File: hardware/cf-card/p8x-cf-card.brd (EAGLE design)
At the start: 160 x 100 mm, 27 parts, among them J1 DIN41612-96M, J2 CF/IDE 40P, U1 DATA BUF, U2 IO PAGE, U3 DOE DEC, U4 DLD DEC, U5 74HCT14, U6 74HCT10, U7 74HCT10, U8 74HCT08, U9 CF HI-BYTE DNP

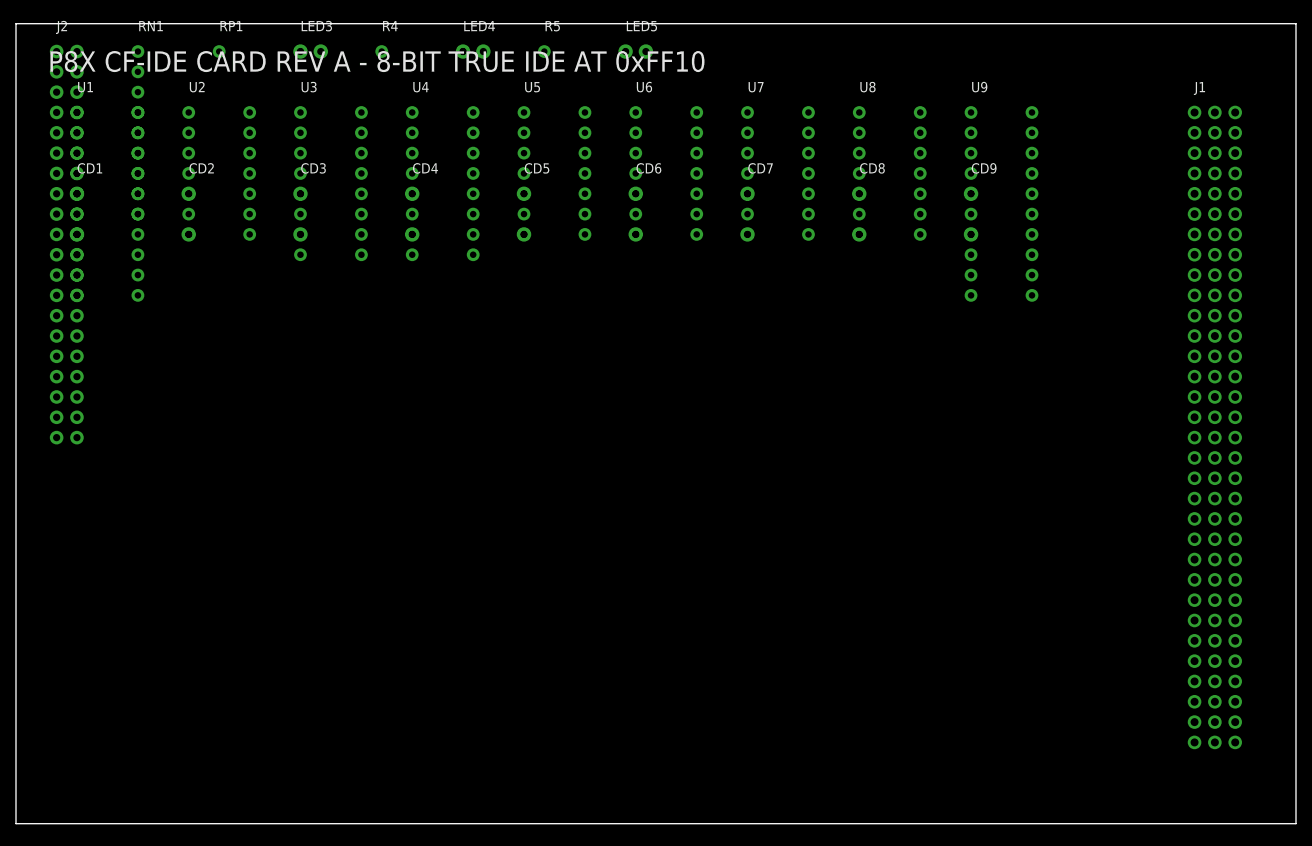
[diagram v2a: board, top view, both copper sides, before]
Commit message: feat(hw): footprint-aware placement (no component overlaps) + overlap guard
The old auto-placer used a fixed 13.97x25.4mm grid that was tighter than real
footprints — tall DIPs collided with the row below and per-IC caps were buried.

- card(): place by each part's real pad-extent + clearance, flowing in rows that
  wrap at the board width and stack downward (J1 hugs the left edge). Guarantees
  no overlaps. Dense cards (ALU, regbank) now run past the 160x100 outline — they
  genuinely don't fit at safe pitch; arrange by hand when routing (the placement
  PDF flags the overflow).
- memory card: relocate the 9 decoupling caps to a clear bottom strip (they sat
  under the tall DIP-28W ICs).
- validate(): add a rotation-aware footprint-overlap guard (board files) so a
  future card can't silently reintroduce overlaps.
- Regenerated all boards + placement/schematic PDFs.

Verified: 0 overlaps across all 7 boards (rotation-aware); 0 validation errors;
all 6 test suites pass.

Co-Authored-By: Claude Opus 4.8 <noreply@anthropic.com>
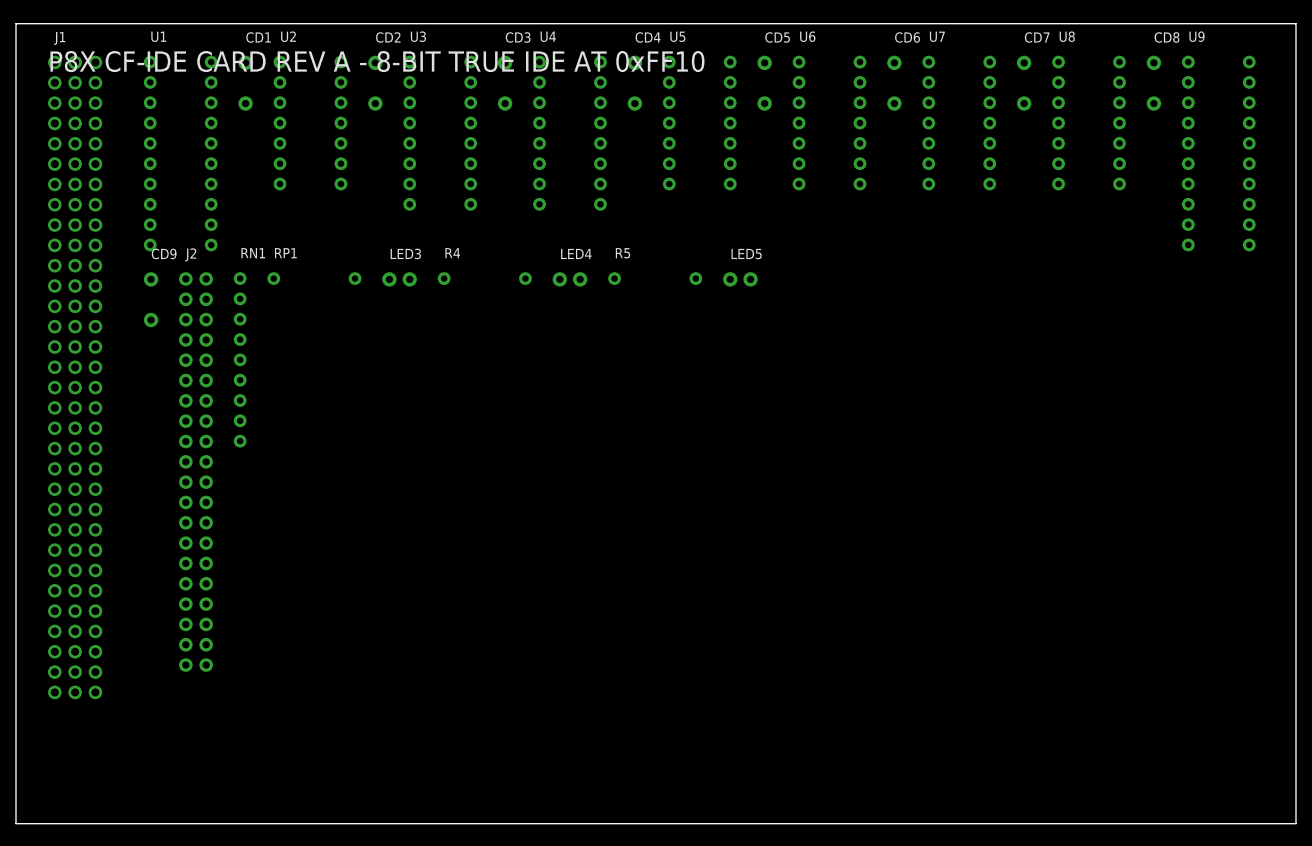
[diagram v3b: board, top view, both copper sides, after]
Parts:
- moved J1 142.6 mm to (4.85, 95.2)
- moved CD9 103.1 mm to (16.9, 68.0)
- moved CD8 40.3 mm to (142.2, 95.1)
- moved CD7 38.3 mm to (126.0, 95.1)
- moved CD6 36.2 mm to (109.8, 95.1)
- moved CD5 34.2 mm to (93.6, 95.1)
- moved J2 32.7 mm to (21.2, 68.1)
- moved CD4 32.3 mm to (77.4, 95.1)
- moved LED5 31.3 mm to (89.3, 68.0)
- moved RN1 31.1 mm to (28.0, 68.1)
- moved LED4 30.9 mm to (68.0, 68.0)
- moved LED3 30.6 mm to (46.7, 68.0)
- moved CD3 30.4 mm to (61.1, 95.1)
- moved R5 29.7 mm to (74.8, 68.1)
- moved R4 29.4 mm to (53.5, 68.1)
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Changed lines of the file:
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@@
 <designrules name="default"><param name="layerSetup" value="(1*2*15*16)"/></designrules>
 <elements>
-<element name="J1" library="p8x" package="DIN96" value="DIN41612-96M" x="147.32" y="88.90"/>
-<element name="U1" library="p8x" package="DIP20" value="DATA BUF" x="7.62" y="88.90"/>
-<element name="CD1" library="p8x" package="C_DISC" value="100N" x="7.62" y="78.74"/>
-<element name="U2" library="p8x" package="DIP14" value="IO PAGE" x="21.59" y="88.90"/>
-<element name="CD2" library="p8x" package="C_DISC" value="100N" x="21.59" y="78.74"/>
-<element name="U3" library="p8x" package="DIP16" value="DOE DEC" x="35.56" y="88.90"/>
-<element name="CD3" library="p8x" package="C_DISC" value="100N" x="35.56" y="78.74"/>
-<element name="U4" library="p8x" package="DIP16" value="DLD DEC" x="49.53" y="88.90"/>
-<element name="CD4" library="p8x" package="C_DISC" value="100N" x="49.53" y="78.74"/>
-<element name="U5" library="p8x" package="DIP14" value="74HCT14" x="63.50" y="88.90"/>
-<element name="CD5" library="p8x" package="C_DISC" value="100N" x="63.50" y="78.74"/>
-<element name="U6" library="p8x" package="DIP14" value="74HCT10" x="77.47" y="88.90"/>
-<element name="CD6" library="p8x" package="C_DISC" value="100N" x="77.47" y="78.74"/>
-<element name="U7" library="p8x" package="DIP14" value="74HCT10" x="91.44" y="88.90"/>
-<element name="CD7" library="p8x" package="C_DISC" value="100N" x="91.44" y="78.74"/>
-<element name="U8" library="p8x" package="DIP14" value="74HCT08" x="105.41" y="88.90"/>
-<element name="CD8" library="p8x" package="C_DISC" value="100N" x="105.41" y="78.74"/>
-<element name="U9" library="p8x" package="DIP20" value="CF HI-BYTE DNP" x="119.38" y="88.90"/>
-<element name="CD9" library="p8x" package="C_DISC" value="100N" x="119.38" y="78.74"/>
-<element name="J2" library="p8x" package="HDR40" value="CF/IDE 40P" x="5.08" y="96.52"/>
-<element name="RN1" library="p8x" package="SIP9" value="8X10K" x="15.24" y="96.52"/>
-<element name="RP1" library="p8x" package="R_AXIAL" value="1K" x="25.40" y="96.52"/>
-<element name="LED3" library="p8x" package="LED5" value="PWR-GRN" x="35.56" y="96.52"/>
-<element name="R4" library="p8x" package="R_AXIAL" value="1K" x="45.72" y="96.52"/>
-<element name="LED4" library="p8x" package="LED5" value="ACT-YEL" x="55.88" y="96.52"/>
-<element name="R5" library="p8x" package="R_AXIAL" value="330R" x="66.04" y="96.52"/>
-<element name="LED5" library="p8x" package="LED5" value="DASP-GRN" x="76.20" y="96.52"/>
+<element name="J1" library="p8x" package="DIN96" value="DIN41612-96M" x="4.85" y="95.15"/>
+<element name="U1" library="p8x" package="DIP20" value="DATA BUF" x="16.78" y="95.20"/>
+<element name="CD1" library="p8x" package="C_DISC" value="100N" x="28.70" y="95.10"/>
+<element name="U2" library="p8x" package="DIP14" value="IO PAGE" x="33.00" y="95.20"/>
+<element name="CD2" library="p8x" package="C_DISC" value="100N" x="44.92" y="95.10"/>
+<element name="U3" library="p8x" package="DIP16" value="DOE DEC" x="49.22" y="95.20"/>
+<element name="CD3" library="p8x" package="C_DISC" value="100N" x="61.14" y="95.10"/>
+<element name="U4" library="p8x" package="DIP16" value="DLD DEC" x="65.44" y="95.20"/>
+<element name="CD4" library="p8x" package="C_DISC" value="100N" x="77.36" y="95.10"/>
+<element name="U5" library="p8x" package="DIP14" value="74HCT14" x="81.66" y="95.20"/>
+<element name="CD5" library="p8x" package="C_DISC" value="100N" x="93.58" y="95.10"/>
+<element name="U6" library="p8x" package="DIP14" value="74HCT10" x="97.88" y="95.20"/>
+<element name="CD6" library="p8x" package="C_DISC" value="100N" x="109.80" y="95.10"/>
+<element name="U7" library="p8x" package="DIP14" value="74HCT10" x="114.10" y="95.20"/>
+<element name="CD7" library="p8x" package="C_DISC" value="100N" x="126.02" y="95.10"/>
+<element name="U8" library="p8x" package="DIP14" value="74HCT08" x="130.32" y="95.20"/>
+<element name="CD8" library="p8x" package="C_DISC" value="100N" x="142.24" y="95.10"/>
+<element name="U9" library="p8x" package="DIP20" value="CF HI-BYTE DNP" x="146.54" y="95.20"/>
+<element name="CD9" library="p8x" package="C_DISC" value="100N" x="16.88" y="68.04"/>
+<element name="J2" library="p8x" package="HDR40" value="CF/IDE 40P" x="21.23" y="68.09"/>
+<element name="RN1" library="p8x" package="SIP9" value="8X10K" x="28.02" y="68.14"/>
+<element name="RP1" library="p8x" package="R_AXIAL" value="1K" x="32.22" y="68.14"/>
+<element name="LED3" library="p8x" package="LED5" value="PWR-GRN" x="46.68" y="68.04"/>
+<element name="R4" library="p8x" package="R_AXIAL" value="1K" x="53.52" y="68.14"/>
+<element name="LED4" library="p8x" package="LED5" value="ACT-YEL" x="67.98" y="68.04"/>
+<element name="R5" library="p8x" package="R_AXIAL" value="330R" x="74.82" y="68.14"/>
+<element name="LED5" library="p8x" package="LED5" value="DASP-GRN" x="89.28" y="68.04"/>
 </elements><signals>
 <signal name="-CFOE">

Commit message: fix(bom): card DIN connectors were undercounted (1 -> 6); label them FABC96R
Two fixes:
- card() built CARDS[name] from `allp`, which omitted J1 — so the 5 plug-in
  cards' DIN41612 edge connectors never reached the BOM (it showed qty 1, only
  the memory card's J1). Include J1 in allp (the schematic renderer already
  filters J1 by name, so rendering is unchanged). BOM now correctly shows 6 card
  connectors + 10 backplane receptacles.
- Card edge connector is FABC96R (user-specified): set the value label on every
  card J1 and name it in the BOM; backplane receptacles noted as the mating part.

Regenerated all boards + PDFs + BOM; all 6 test suites pass.

Co-Authored-By: Claude Opus 4.8 <noreply@anthropic.com>
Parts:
- J1: value DIN41612-96M -> FABC96R
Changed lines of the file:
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@@
 <designrules name="default"><param name="layerSetup" value="(1*2*15*16)"/></designrules>
 <elements>
-<element name="J1" library="p8x" package="DIN96" value="DIN41612-96M" x="4.85" y="95.15"/>
+<element name="J1" library="p8x" package="DIN96" value="FABC96R" x="4.85" y="95.15"/>
 <element name="U1" library="p8x" package="DIP20" value="DATA BUF" x="16.78" y="95.20"/>
 <element name="CD1" library="p8x" package="C_DISC" value="100N" x="28.70" y="95.10"/>
